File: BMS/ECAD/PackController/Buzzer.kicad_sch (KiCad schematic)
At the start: 5 parts, among them Q15 2N7002

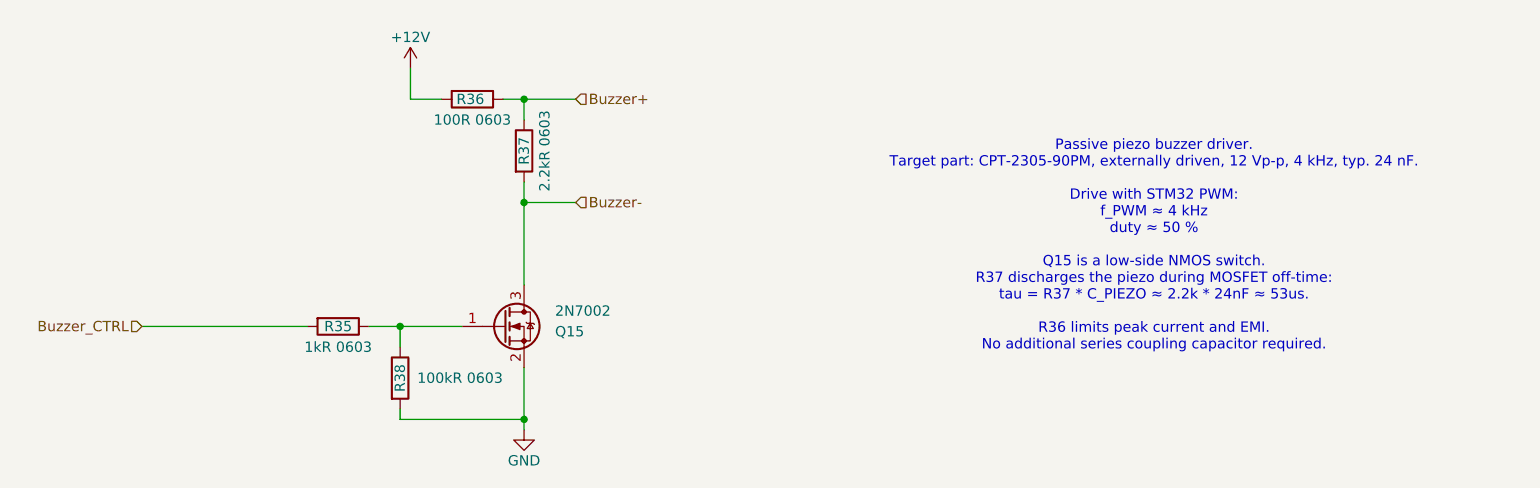
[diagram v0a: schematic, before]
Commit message: finished schemativ of precharge
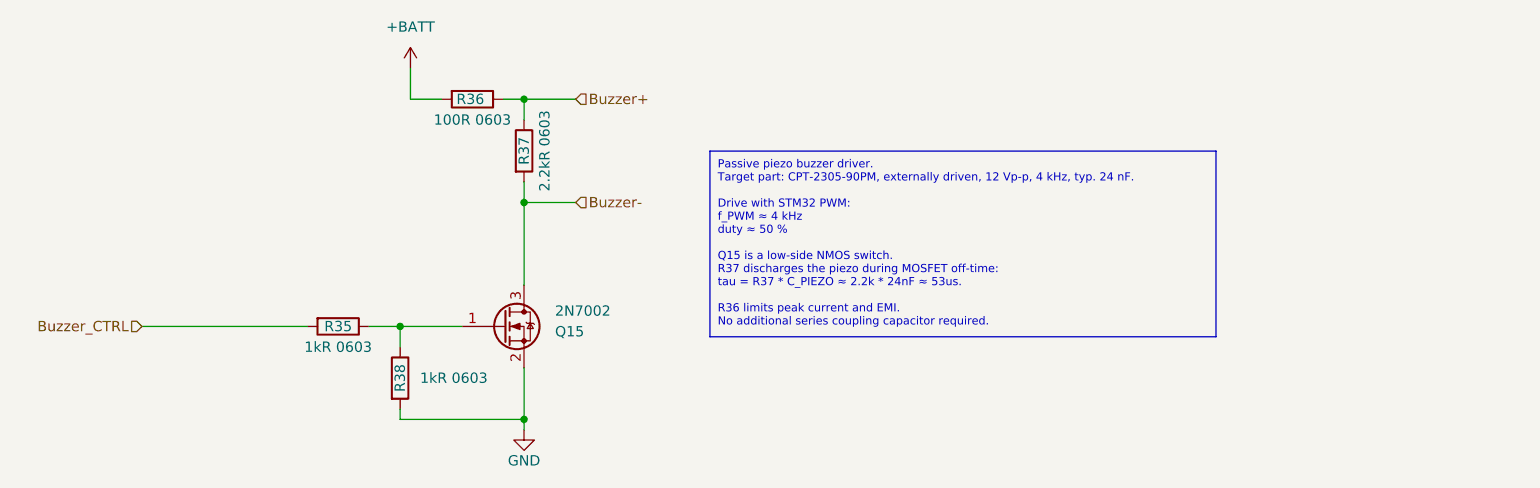
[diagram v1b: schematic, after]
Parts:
- R38: value 100kR 0603 -> 1kR 0603
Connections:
- net +12V renamed +BATT
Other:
- note removed: "Passive piezo buzzer driver. Target part: CPT-2305-90PM, externally driven, 12 Vp-p, 4 kHz, typ. 24 nF. Drive with STM32 PWM: f_PWM ≈ 4 kHz duty ≈ 50 % Q15 is a low-side NMOS switch. R37 discharges the piezo during MOSFET off-time: tau = R37 * C_PIEZO ≈ 2.2k * 24nF ≈ 53us. R36 limits peak current and EMI. No additional series coupling capacitor required."
- company: (none) -> Lukas Elektronik
- title: (none) -> PackController
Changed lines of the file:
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@@
 	(generator_version "10.0")
 	(paper "A4")
-	(text "Passive piezo buzzer driver.\nTarget part: CPT-2305-90PM, externally driven, 12 Vp-p, 4 kHz, typ. 24 nF.\n\nDrive with STM32 PWM:\nf_PWM ≈ 4 kHz\nduty ≈ 50 %\n\nQ15 is a low-side NMOS switch.\nR37 discharges the piezo during MOSFET off-time:\ntau = R37 * C_PIEZO ≈ 2.2k * 24nF ≈ 53us.\n\nR36 limits peak current and EMI.\nNo additional series coupling capacitor required."
+	(title_block
+		(title "PackController")
+		(date "2026-03-03")
+		(rev "V0.9")
+		(company "Lukas Elektronik")
+	)
+	(text_box "Passive piezo buzzer driver.\nTarget part: CPT-2305-90PM, externally driven, 12 Vp-p, 4 kHz, typ. 24 nF.\n\nDrive with STM32 PWM:\nf_PWM ≈ 4 kHz\nduty ≈ 50 %\n\nQ15 is a low-side NMOS switch.\nR37 discharges the piezo during MOSFET off-time:\ntau = R37 * C_PIEZO ≈ 2.2k * 24nF ≈ 53us.\n\nR36 limits peak current and EMI.\nNo additional series coupling capacitor required."
 		(exclude_from_sim no)
-		(at 222.25 90.424 0)
+		(at 167.64 78.7669 0)
+		(size 62.23 22.8331)
+		(margins 0.9525 0.9525 0.9525 0.9525)
+		(stroke
+			(width 0)
+			(type solid)
+			(color 0 0 0 1)
+		)
+		(fill
+			(type color)
+			(color 255 255 194 1)
+		)
 		(effects
 			(font
-				(size 1.27 1.27)
-			)
+				(size 1 1)
+				(color 0 0 0 1)
+			)
+			(justify left top)
 		)
 	)
@@
 			)
 		)
-		(property "Value" "100kR 0603"
-			(at 136.906 106.68 0)
+		(property "Value" "1kR 0603"
+			(at 136.144 106.68 0)
 			(show_name no)
 			(do_not_autoplace no)
@@
 				(path "/58a1c93e-baba-4d23-9191-955e00968735/9e76a46f-aff0-416c-bf65-690935f0ea58"
 					(reference "R38")
-					(unit 1)
-				)
-			)
-		)
-	)
-	(symbol
-		(lib_id "power:+3.3V")
-		(at 130.81 68.58 0)
-		(unit 1)
-		(body_style 1)
-		(exclude_from_sim no)
-		(in_bom yes)
-		(on_board yes)
-		(in_pos_files yes)
-		(dnp no)
-		(property "Reference" "#PWR014"
-			(at 130.81 72.39 0)
-			(hide yes)
-			(show_name no)
-			(do_not_autoplace no)
-			(effects
-				(font
-					(size 1.27 1.27)
-				)
-			)
-		)
-		(property "Value" "+12V"
-			(at 130.81 64.77 0)
-			(show_name no)
-			(do_not_autoplace no)
-			(effects
-				(font
-					(size 1.27 1.27)
-				)
-			)
-		)
-		(property "Footprint" ""
-			(at 130.81 68.58 0)
-			(hide yes)
-			(show_name no)
-			(do_not_autoplace no)
-			(effects
-				(font
-					(size 1.27 1.27)
-				)
-			)
-		)
-		(property "Datasheet" ""
-			(at 130.81 68.58 0)
-			(hide yes)
-			(show_name no)
-			(do_not_autoplace no)
-			(effects
-				(font
-					(size 1.27 1.27)
-				)
-			)
-		)
-		(property "Description" ""
-			(at 130.81 68.58 0)
-			(show_name no)
-			(do_not_autoplace no)
-			(effects
-				(font
-					(size 1.27 1.27)
-				)
-			)
-		)
-		(pin "1"
-		)
-		(instances
-			(project "Pack_Controller"
-				(path "/58a1c93e-baba-4d23-9191-955e00968735/9e76a46f-aff0-416c-bf65-690935f0ea58"
-					(reference "#PWR014")
 					(unit 1)
 				)
@@
 					(unit 1)
 				)
+			)
+		)
+	)
+	(symbol
+		(lib_id "power:+BATT")
+		(at 130.81 68.58 0)
+		(unit 1)
+		(body_style 1)
+		(exclude_from_sim no)
+		(in_bom yes)
+		(on_board yes)
+		(in_pos_files yes)
+		(dnp no)
+		(fields_autoplaced yes)
+		(property "Reference" "#PWR038"
+			(at 130.81 72.39 0)
+			(hide yes)
+			(show_name no)
+			(do_not_autoplace no)
+			(effects
+				(font
+					(size 1.27 1.27)
+				)
+			)
+		)
+		(property "Value" "+BATT"
+			(at 130.81 63.5 0)
+			(show_name no)
+			(do_not_autoplace no)
+			(effects
+				(font
+					(size 1.27 1.27)
+				)
+			)
+		)
+		(property "Footprint" ""
+			(at 130.81 68.58 0)
+			(hide yes)
+			(show_name no)
+			(do_not_autoplace no)
+			(effects
+				(font
+					(size 1.27 1.27)
+				)
+			)
+		)
+		(property "Datasheet" ""
+			(at 130.81 68.58 0)
+			(hide yes)
+			(show_name no)
+			(do_not_autoplace no)
+			(effects
+				(font
+					(size 1.27 1.27)
+				)
+			)
+		)
+		(property "Description" ""
+			(at 130.81 68.58 0)
+			(show_name no)
+			(do_not_autoplace no)
+			(effects
+				(font
+					(size 1.27 1.27)
+				)
+			)
+		)
+		(pin "1"
+		)
+		(instances
+			(project "Pack_Controller"
+				(path "/58a1c93e-baba-4d23-9191-955e00968735/9e76a46f-aff0-416c-bf65-690935f0ea58"
+					(reference "#PWR038")
+					(unit 1)
+				)
